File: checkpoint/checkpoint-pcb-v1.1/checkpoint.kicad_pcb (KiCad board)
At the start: 4 copper layers, 85.2 x 39.6 mm, 113 parts, among them J1 T0, J10 CAN_OUT, J11 BOOT, J12 Y_ENDSTOP, J13 I2C, J14 SERVO, J15 RGB, J16 SWD, J17 USB_C_Receptacle_USB2.0_16P, J18 PWR_OUT, J19 PWR_CAN_IN, J2 T1, J3 T2, J4 T3, J5 2_WIRE, J6 24_3_WIRE_A, J7 PT100, J8 23_WIRE, J9 PT100_1K, Q1 BSS138, SW1 SW_RESET, U1 MAX31865xTP, U2 SN65HVD1050D, U3 STM32G0B1CBTx, U4 USBLC6-2P6, U5 AMS1117-3.3, U6 TPS5430DDA, Y1 Crystal

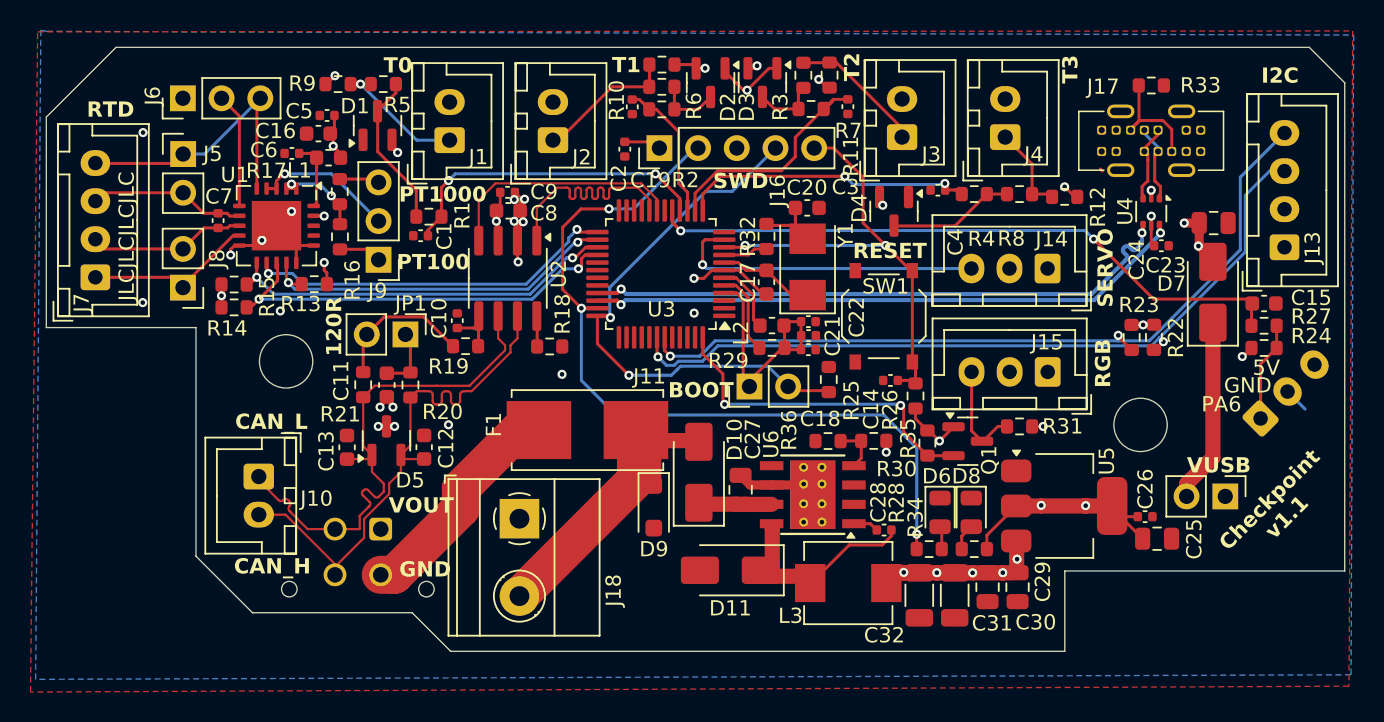
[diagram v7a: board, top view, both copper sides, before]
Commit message: chore: remove reference designators and clean up silkscreen
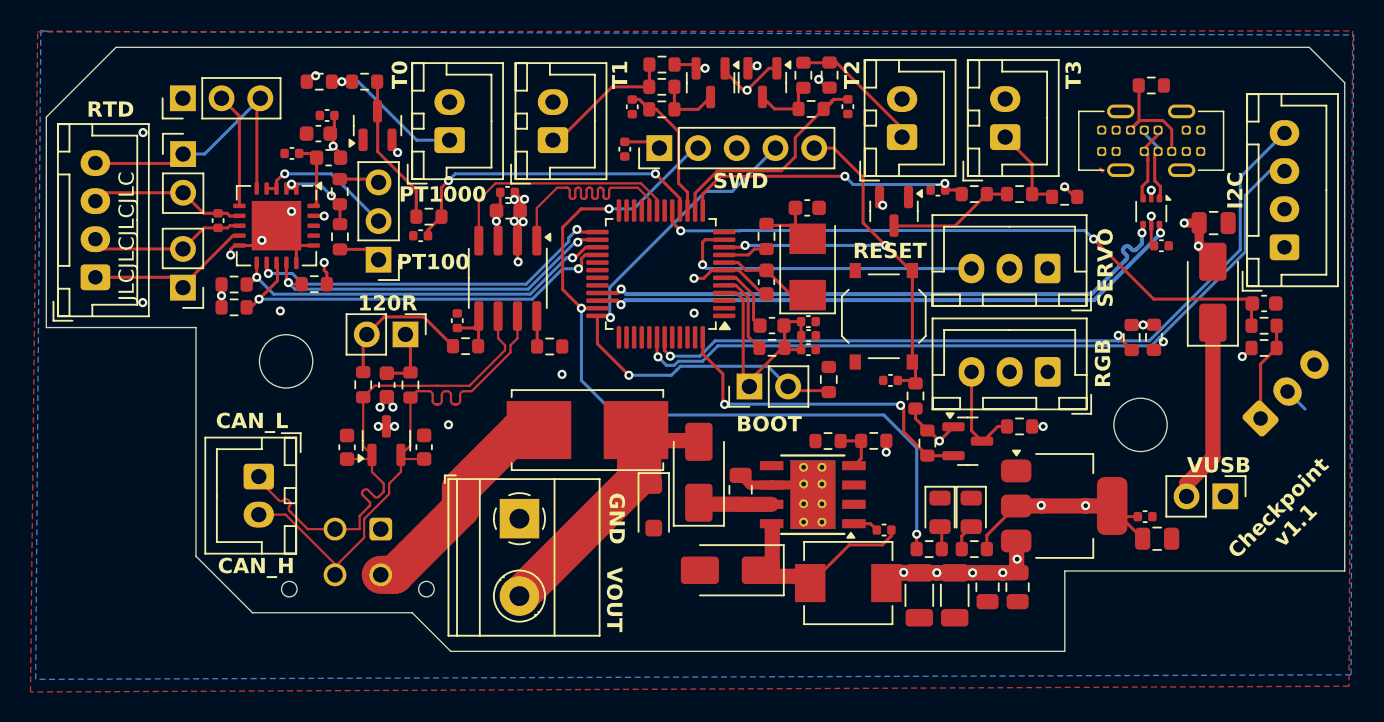
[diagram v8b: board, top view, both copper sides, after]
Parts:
- moved R5 1.24 mm to (43.0, 36.3)
- moved R9 1.24 mm to (40.1, 36.3)
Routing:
- net Net-(J1-Pin_1): track 8.37 -> 9.98 mm
